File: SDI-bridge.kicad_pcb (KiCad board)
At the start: 4 copper layers, 68 x 33 mm, 173 parts, among them J1 031-70526-21, J2 031-70526-21, J3 WE_68715014522_ONE-SIDE, J4 MC-HVT1-S04-G, J5 MC-HVT1-S04-G, U1 MAX8902B, U2 GS2971A, U3 GS2988, U4 CrossLink_LIF-MD6000-6JMG80I, U5 SC18IS602BIPW, Y1 ABM7_27.000MH_D2Y_T

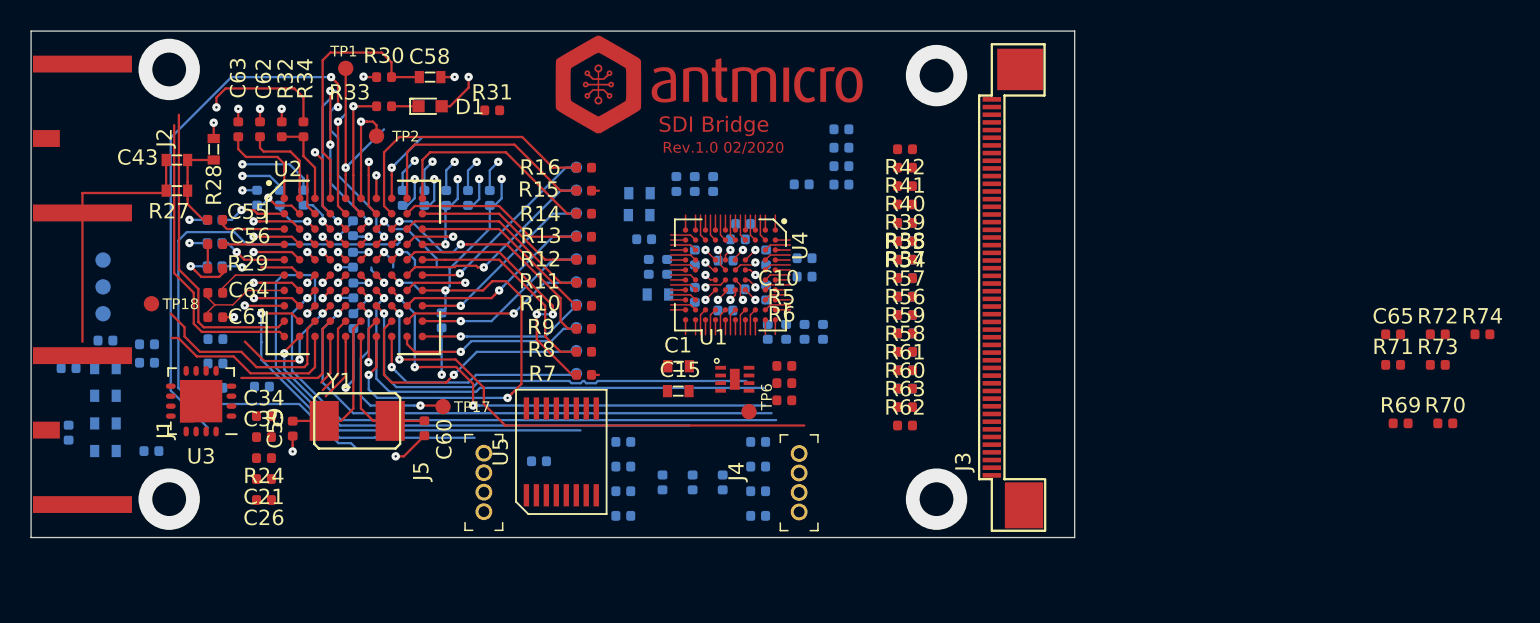
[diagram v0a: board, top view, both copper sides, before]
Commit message: Add routing on 6 layers
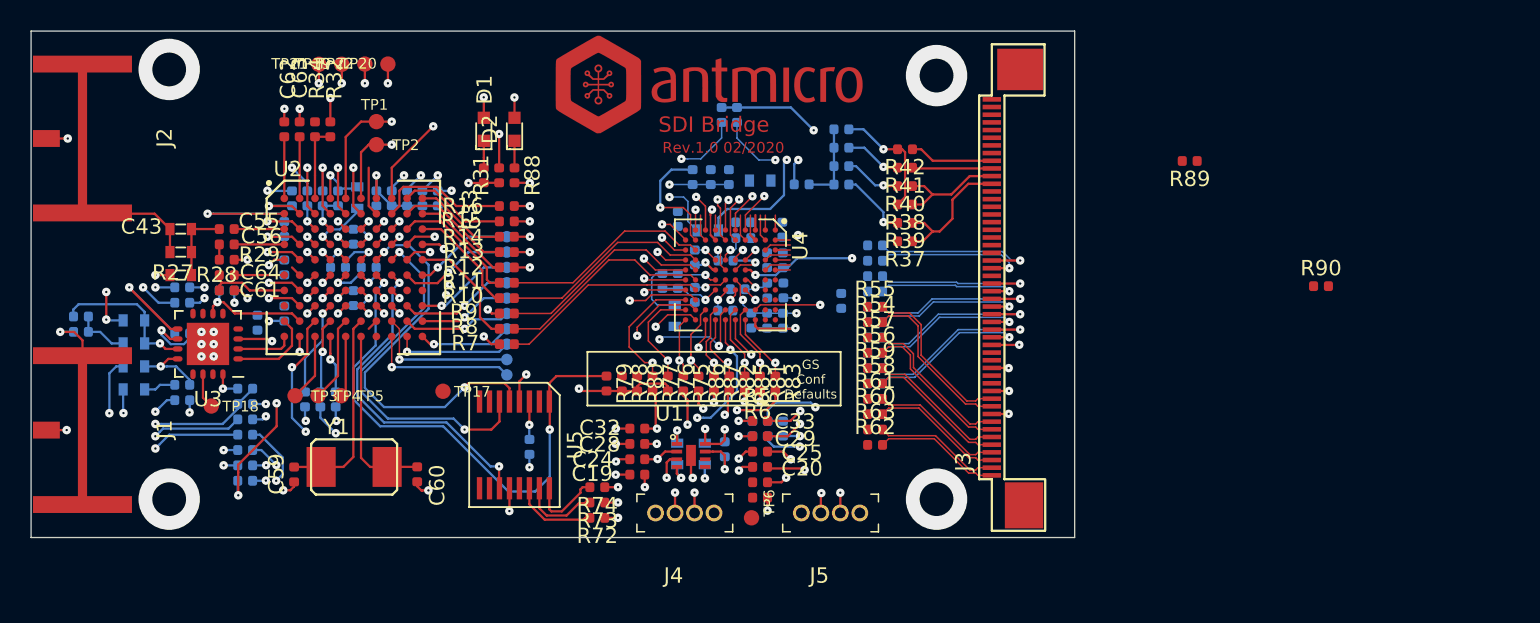
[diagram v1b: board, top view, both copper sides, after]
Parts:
- added D2: LG_L29K-G2J1-24-Z, antmicro-footprints:LED_0603, F.Cu at (131.5, 106.4)
- added R75: R_0R_0402, antmicro-footprints:0402-res, F.Cu at (142.5, 123.0)
- added R76: R_0R_0402, antmicro-footprints:0402-res, F.Cu at (141.5, 123.0)
- added R77: R_0R_0402, antmicro-footprints:0402-res, F.Cu at (140.5, 123.0)
- added R78: R_0R_0402, antmicro-footprints:0402-res, F.Cu at (138.5, 123.0)
- added R79: R_0R_0402, antmicro-footprints:0402-res, F.Cu at (137.5, 123.0)
- added R80: R_0R_0402, antmicro-footprints:0402-res, F.Cu at (139.5, 123.0)
- added R81: R_0R_0402, antmicro-footprints:0402-res, F.Cu at (147.5, 123.0)
- added R82: R_0R_0402, antmicro-footprints:0402-res, F.Cu at (145.5, 123.0)
- added R83: R_0R_0402, antmicro-footprints:0402-res, F.Cu at (148.5, 123.0)
- added R84: R_0R_0402, antmicro-footprints:0402-res, B.Cu at (112.8, 116.9)
- added R85: R_0R_0402, antmicro-footprints:0402-res, F.Cu at (146.5, 123.0)
- added R86: R_0R_0402, antmicro-footprints:0402-res, F.Cu at (143.5, 123.0)
- added R87: R_0R_0402, antmicro-footprints:0402-res, F.Cu at (144.5, 123.0)
- added R88: R_100R_0402, antmicro-footprints:0402-res, F.Cu at (131.5, 109.4)
- added R89: R_0R_0402, antmicro-footprints:0402-res, F.Cu at (175.5, 108.5)
- added R90: R_0R_0402, antmicro-footprints:0402-res, F.Cu at (184.1, 116.6)
- added R91: R_0R_0402, antmicro-footprints:0402-res, B.Cu at (152.8, 117.6)
- added TP19: TP_SMD1MM, antmicro-footprints:Testpoint_smd_1mm, F.Cu at (120.2, 102.2)
- added TP20: TP_SMD1MM, antmicro-footprints:Testpoint_smd_1mm, F.Cu at (123.2, 102.2)
- added TP21: TP_SMD1MM, antmicro-footprints:Testpoint_smd_1mm, F.Cu at (118.8, 102.2)
- added TP22: TP_SMD1MM, antmicro-footprints:Testpoint_smd_1mm, F.Cu at (121.8, 102.2)
- C1, C10, C15, C21, C26, C30, C34, C58, C65, R24, R30, R69, R70, R71: moved to B.Cu
- C19, C20, C24, C25, C28, C29, C32, C33, TP3, TP4, TP5: moved to F.Cu
- moved C65 79.0 mm to (109.8, 124.0), turned to 180 degrees
- moved R71 74.8 mm to (114.0, 123.3), turned to 180 degrees
- moved R74 58.5 mm to (136.9, 129.7), turned to 180 degrees
- moved R72 56.1 mm to (136.9, 131.7), turned to 180 degrees
- moved R73 55.5 mm to (136.9, 130.7), turned to 180 degrees
- moved R70 50.3 mm to (146.0, 105.5), turned to 270 degrees
- moved R69 48.6 mm to (145.0, 105.5), turned to 270 degrees
- moved J5 24.5 mm to (154.0, 131.4), turned to 180 degrees
- moved R25 16.5 mm to (114.0, 129.3), turned to 180 degrees
- moved TP5 16.4 mm to (120.2, 123.7)
- moved TP4 15.7 mm to (118.7, 123.7)
- moved TP3 15.3 mm to (117.2, 123.7)
- moved C36 9.83 mm to (109.8, 119.7), turned to 180 degrees
- moved C58 9.18 mm to (121.2, 110.8), turned to 270 degrees
- moved R28 8.48 mm to (109.8, 115.9), turned to 180 degrees
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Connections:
- net /LOCKED_IN renamed /LOCKED_CL
- net /VCCGPLL renamed VCCGPLL
- net Net-(R36-Pad1) renamed /CDONE
- C30 pad 1: CD_VDD -> VDD
- C34 pad 1: CD_VDD -> VDD
- C37 pad 1: /VCCIO -> VCC_IO
- C41 pad 1: /VCCIO -> VCC_IO
- C46 pad 1: /VCCIO -> VCC_IO
- C50 pad 1: /VCCIO -> VCC_IO
- C54 pad 1: /VCCIO -> VCC_IO
- C57 pad 1: /VCCIO -> VCC_IO
- FB1 pad 2: /VCCIO -> VCC_IO
- J1 pad 2: GND -> GNDA
- J2 pad 2: GND -> GNDA
- R20 pad 1: GND -> GNDA
- R24 pad 2: CD_VDD -> VDD
- U4 pad D2: VCCA_DPHY -> Net-(R90-Pad2)
- U4 pad D4: VCCA_DPHY -> Net-(R90-Pad2)
- U4 pad D7: VCCA_DPHY -> Net-(R91-Pad2)
- U4 pad E7: VCCA_DPHY -> Net-(R91-Pad2)
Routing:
- net /SCL_CL: track 0.98 -> 59.3 mm, vias 0 -> 3
- net /SDA_CL: track 0.98 -> 51.7 mm, vias 0 -> 3
- net /Y_1ANC: track 10.3 -> 59.5 mm, vias 1 -> 4
- net VDD: track 0.00 -> 39.5 mm, vias 0 -> 10
- net /F_DE: track 8.67 -> 48.1 mm, vias 1 -> 4
- net /~CS~_TMS: track 2.05 -> 34.8 mm, vias 1 -> 2
- net /RST_TRST: track 6.68 -> 39.0 mm, vias 1 -> 2
- net +3V3: track 3.84 -> 33.0 mm, vias 2 -> 14
- net /AUDIO_SERIAL_BIT_CLK: track 0.98 -> 30.1 mm, vias 0 -> 2
- net /AUDIO_WORD_CLK: track 1.76 -> 29.9 mm, vias 0 -> 2
- net /SCL_GS: track 0.00 -> 27.7 mm, vias 0 -> 2
- net GNDREF: track 48.3 -> 75.5 mm, vias 24 -> 39
- net /AUDIO_MASTER_CLK: track 1.76 -> 27.9 mm, vias 0 -> 2
- net /PCLK: track 5.80 -> 31.4 mm, vias 1 -> 2
- net /SDA_GS: track 0.00 -> 25.1 mm, vias 0 -> 2
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- added copper zone on In4.Cu, net /GNDGPLL
- added copper zone on In4.Cu, net /GNDPLL_DPHY
- added copper zone on In4.Cu, net GNDA
- added copper zone on In4.Cu, net GNDREF
- added copper zone on In1.Cu, net IO_VDD
- added copper zone on In1.Cu, net VCC_IO
- added copper zone on In1.Cu, net VDD
- removed copper zone on In1.Cu, net +VSW
- removed copper zone on In2.Cu, net GNDA
- removed copper zone on In2.Cu, net GNDREF
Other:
- copper layers 4 -> 6
- net class Default: via_dia 0.55 -> 0.55625
- net class Default2 added: clearance 0.1, trace_width 0.1, via_dia 0.55625, via_drill 0.15
- net class Inner_Layer added: clearance 0.1, trace_width 0.2, via_dia 0.55625, via_drill 0.15
- net class Power_supply removed
- board text added: "GS Conf Defaults"

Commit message: Complete pcb routing
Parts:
- R89, R90: moved to B.Cu
- moved R90 36.3 mm to (147.9, 112.9), turned to 270 degrees
- moved R89 30.7 mm to (144.8, 107.9)
- moved R22 13.3 mm to (134.7, 127.1), turned to 90 degrees
- moved R21 10.1 mm to (137.0, 127.1), turned to 90 degrees
- moved C49 9.05 mm to (148.1, 108.0), turned to 90 degrees
- moved R91 7.67 mm to (145.3, 119.3), turned to 0 degrees
- moved R44 6.55 mm to (156.9, 108.7)
- moved R45 6.55 mm to (156.9, 107.7)
- moved R46 6.55 mm to (156.9, 110.7)
- moved R47 6.55 mm to (156.9, 109.7)
- moved R48 6.55 mm to (156.9, 112.7)
- moved R49 6.55 mm to (156.9, 111.7)
- moved R50 6.55 mm to (156.9, 114.7)
- moved R51 6.55 mm to (156.9, 113.7)
- moved R52 6.55 mm to (156.9, 116.7)
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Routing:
- net VCCA_DPHY: track 0.00 -> 44.9 mm, vias 0 -> 4
- net GNDREF: track 75.5 -> 117.7 mm, vias 39 -> 49
- net /DATA_ERRORb: track 14.8 -> 47.5 mm
- net +1V2: track 30.3 -> 59.1 mm, vias 14 -> 15
- net /SCL_GS: track 27.7 -> 55.4 mm, vias 2 -> 3
- net /SDA_GS: track 25.1 -> 52.7 mm, vias 2 -> 3
- net /DPHY0_D2_P: track 0.00 -> 18.3 mm, vias 0 -> 2
- net /DPHY0_D3_P: track 0.00 -> 18.3 mm, vias 0 -> 2
- net /DPHY0_D3_N: track 0.00 -> 17.6 mm, vias 0 -> 2
- net /DPHY0_D2_N: track 0.00 -> 17.3 mm, vias 0 -> 2
- net /IOPROC_EN_~DIS~: track 33.8 -> 50.7 mm
- net /Audio_EN_~DIS~: track 32.4 -> 47.9 mm
- net /DPHY0_D1_P: track 0.00 -> 13.4 mm, vias 0 -> 2
- net /DPHY0_D1_N: track 0.00 -> 12.8 mm, vias 0 -> 2
- net /DPHY0_D0_P: track 0.00 -> 12.3 mm, vias 0 -> 2
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- added copper zone on In1.Cu, net VCCA_DPHY
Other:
- net class Default: trace_width 0.1 -> 0.125; via_dia 0.55625 -> 0.55
- net class Default2 removed
- net class Inner_Layer: via_dia 0.55625 -> 0.55

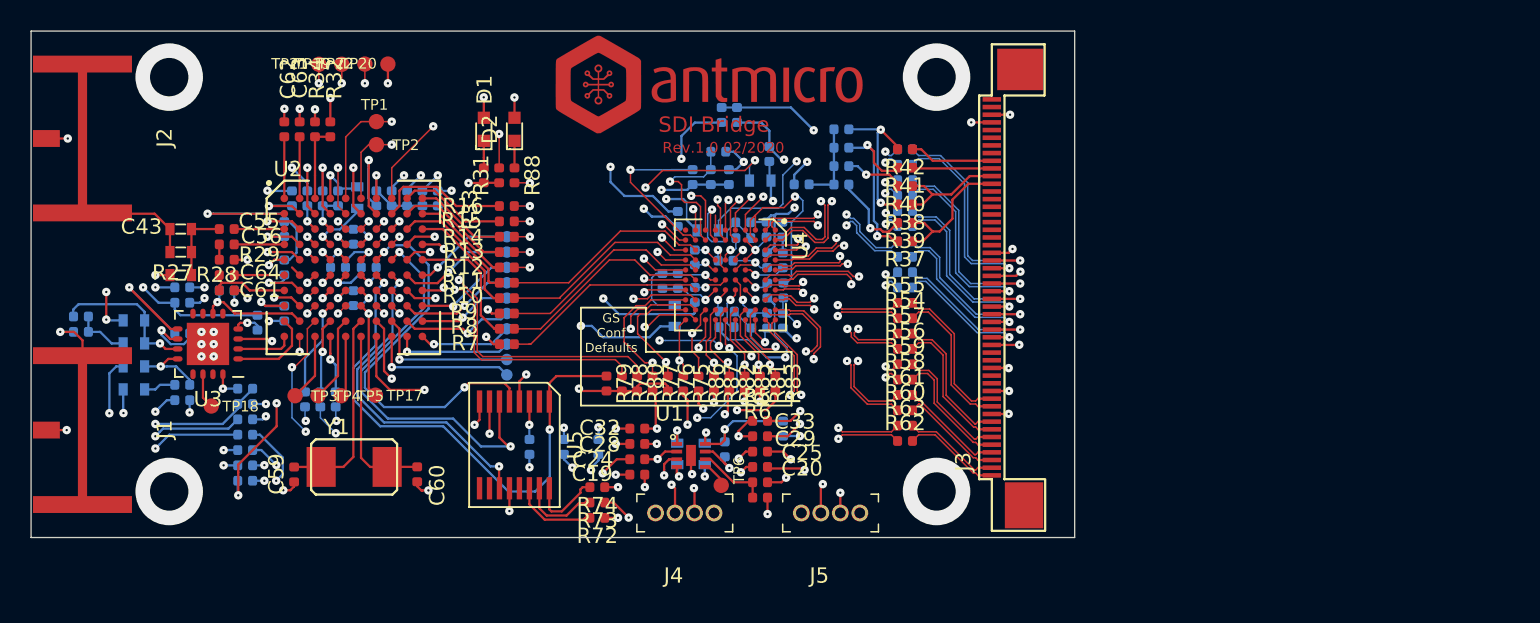
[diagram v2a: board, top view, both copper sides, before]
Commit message: Clean up designators
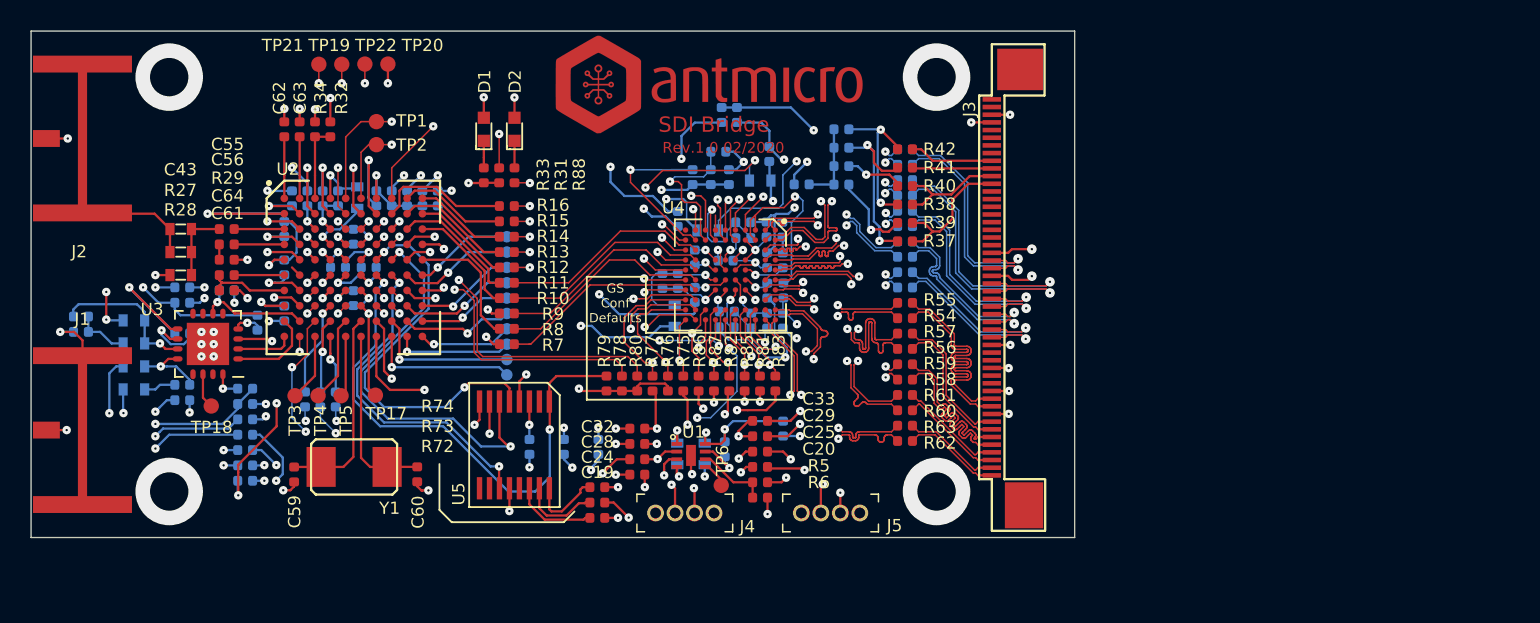
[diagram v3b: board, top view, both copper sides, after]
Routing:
- net /MIPI0_CLK_N: track 9.79 -> 15.4 mm
- net /MIPI0_CLK_P: track 9.79 -> 15.4 mm
- net /MIPI1_D0_N: track 12.7 -> 18.2 mm
- net /DPHY0_D0_N: track 11.2 -> 15.9 mm
- net /MIPI1_D0_P: track 14.0 -> 18.2 mm
- net /DPHY0_D0_P: track 12.3 -> 15.9 mm
- net /MIPI0_D1_P: track 8.14 -> 11.7 mm
- net /MIPI0_D1_N: track 8.14 -> 11.7 mm
- net /MIPI1_D1_N: track 11.6 -> 14.1 mm
- net /MIPI1_D3_N: track 9.12 -> 11.5 mm
- net GNDREF: track 117.7 -> 119.6 mm
- net /MIPI1_D2_N: track 10.3 -> 11.8 mm
- net /MIPI1_CLK_N: track 13.4 -> 14.7 mm
- net /DPHY0_D3_N: track 17.6 -> 18.8 mm
- net /MIPI1_D1_P: track 12.9 -> 14.1 mm
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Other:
- net class Default: via_dia 0.55 -> 0.625
- net class Inner_Layer: via_dia 0.55 -> 0.625
- board text removed: "JTAG"

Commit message: Fix inner layer clearance and tracks width
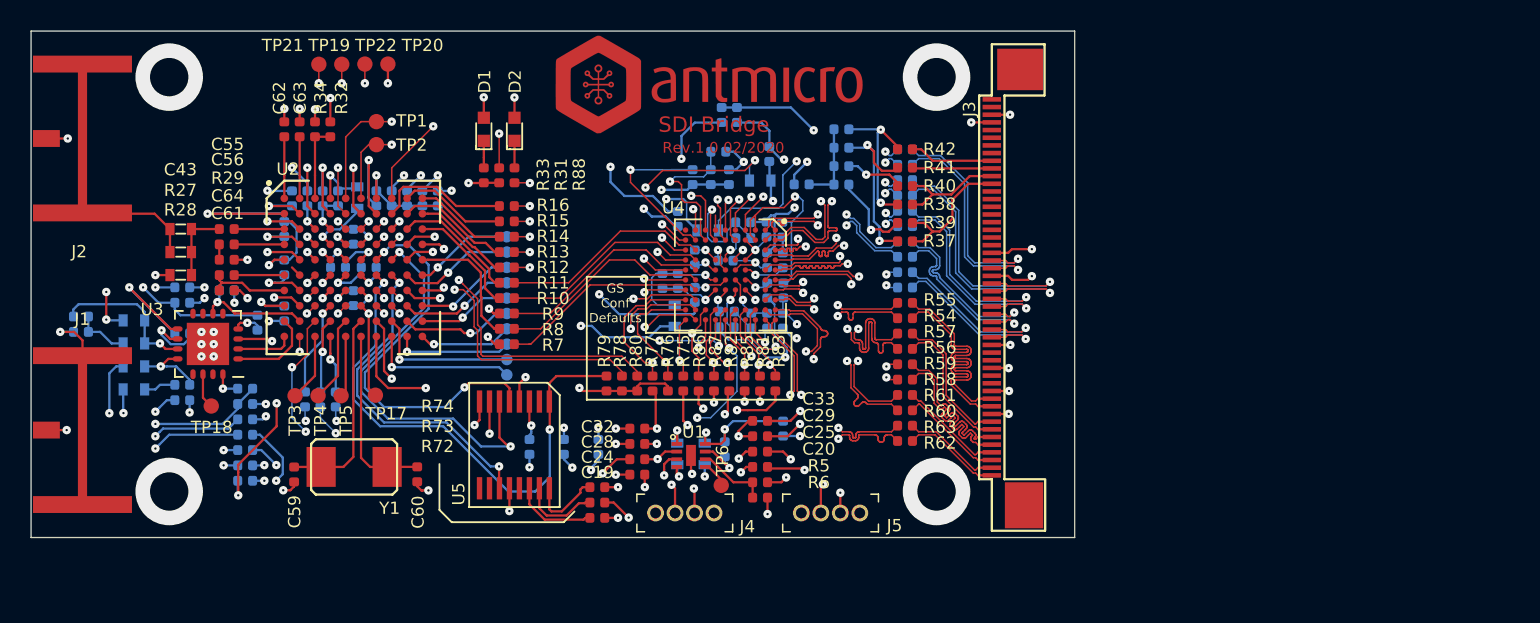
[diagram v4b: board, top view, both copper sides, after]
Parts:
- C1, C15, C58: footprint antmicro-footprints:0603-cap -> SDI-bridge-footprints:0603-cap
- C10, C11, C12, C13, C14, C16, C17, C18, C19, C2, C20, C21, C22, C23, C24, C25, C26, C28, C29, C3, C30, C31, C32, C33, C34, C35, C36, C37, C38, C39, C4, C40, C41, C42, C44, C45, C46, C47, C48, C49, C5, C50, C51, C52, C53, C54, C55, C56, C57, C6, C61, C62, C63, C64, C65, C7, C8, C9: footprint antmicro-footprints:0402-cap -> SDI-bridge-footprints:0402-cap
- C27, C59, C60, R1, R10, R11, R12, R13, R14, R15, R16, R2, R21, R22, R23, R24, R25, R26, R29, R3, R30, R31, R32, R33, R34, R35, R36, R37, R38, R39, R4, R40, R41, R42, R43, R44, R45, R46, R47, R48, R49, R5, R50, R51, R52, R53, R54, R55, R56, R57, R58, R59, R6, R60, R61, R62, R63, R64, R65, R66, R67, R68, R69, R7, R70, R71, R72, R73, R74, R75, R76, R77, R78, R79, R8, R80, R81, R82, R83, R84, R85, R86, R87, R88, R89, R9, R90, R91: footprint antmicro-footprints:0402-res -> SDI-bridge-footprints:0402-res
- C43, FB1, FB2, FB3, R17, R18, R19, R20, R27, R28: footprint antmicro-footprints:0603-res -> SDI-bridge-footprints:0603-res
- D1, D2: footprint antmicro-footprints:LED_0603 -> SDI-bridge-footprints:LED_0603
- J1, J2: footprint antmicro-footprints:BNC_Edge_Conn -> SDI-bridge-footprints:BNC_Edge_Conn
- J3: footprint antmicro-footprints:WE_68715014522_ONE-SIDE -> SDI-bridge-footprints:WE_68715014522_ONE-SIDE
- J4, J5: footprint antmicro-footprints:PinHeader_1x4_P1.27mm_Drill.7mm -> SDI-bridge-footprints:PinHeader_1x4_P1.27mm_Drill.7mm
- N1: footprint antmicro-footprints:antmicro-logo_scaled_20mm -> SDI-bridge-footprints:antmicro-logo_scaled_20mm
- TP1, TP17, TP18, TP19, TP2, TP20, TP21, TP22, TP3, TP4, TP5, TP6: footprint antmicro-footprints:Testpoint_smd_1mm -> SDI-bridge-footprints:Testpoint_smd_1mm
- TP10, TP11, TP12, TP13, TP14, TP15, TP16, TP7, TP8, TP9: footprint antmicro-footprints:Testpoint_smd_0_75mm -> SDI-bridge-footprints:Testpoint_smd_0_75mm
- U1: footprint antmicro-footprints:TDFN2x2 -> SDI-bridge-footprints:TDFN2x2
- U2: footprint antmicro-footprints:BGA100_11x11mm -> SDI-bridge-footprints:BGA100_11x11mm
- U3: footprint antmicro-footprints:QFN-16_EP_4x4_Pitch0.65mm -> SDI-bridge-footprints:QFN-16_EP_4x4_Pitch0.65mm
- U4: footprint antmicro-footprints:BGA-80pin_ckfBGA80_7.0x7.0mm -> SDI-bridge-footprints:BGA-80pin_ckfBGA80_7.0x7.0mm
- U5: footprint antmicro-footprints:SC18IS602B -> SDI-bridge-footprints:SC18IS602B
- Y1: footprint antmicro-footprints:ABM7_OSC -> SDI-bridge-footprints:ABM7_OSC
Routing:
- net /DOUT15: track 11.9 -> 14.0 mm
- net /DOUT16: track 11.9 -> 13.1 mm
- net /DPHY0_D1_N: track 13.4 -> 12.3 mm
- net /DPHY0_D1_P: track 13.4 -> 12.6 mm
- net /D12: track 11.1 -> 11.8 mm
- net /F_DE: track 47.9 -> 48.4 mm
